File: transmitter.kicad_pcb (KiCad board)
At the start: 6 copper layers, 200 x 110 mm, 244 parts, among them IC1 W9864G6KH-6, IC2 TPS61165DBVR, IC3 MT25QL128ABA1ESE-0SIT, IC4 USBLC6-2SC6, J1 AFC01-S40FCA-00, J2 AFC07-S10ECC-00, J3 B2B-PH-K-S, J4 B2B-PH-K-S, J5 B3B-PH-K-S, J6 USB4085-GF-A, J7 Conn_01x05, J9 Conn_02x06_Odd_Even, Q1 AO3400A, Q2 AO3400A, Q3 SI2301CDS-T1-GE3, Q4 AO3400A, SW1 Button SPST SMD Tactile Switch, SW2 Button SPST SMD Tactile Switch, SW3 Button SPST SMD Tactile Switch, SW4 Button SPST SMD Tactile Switch, SW5 Button SPST SMD Tactile Switch, SW6 Button SPST SMD Tactile Switch, SW7 SW_SPDT_MSM, SW8 Button SPST SMD Tactile Switch, SW9 RotaryEncoder_Switch, U1 STM32H743ZIT6TR, U2 CAT24C256, U3 MP2667GG-0000-Z, U4 AMS1117-3.3, U5 TPS61252DSG, U6 PCA9554APW, Y1 32.768KHZ, Y2 X322525MOB4SI-25MHz

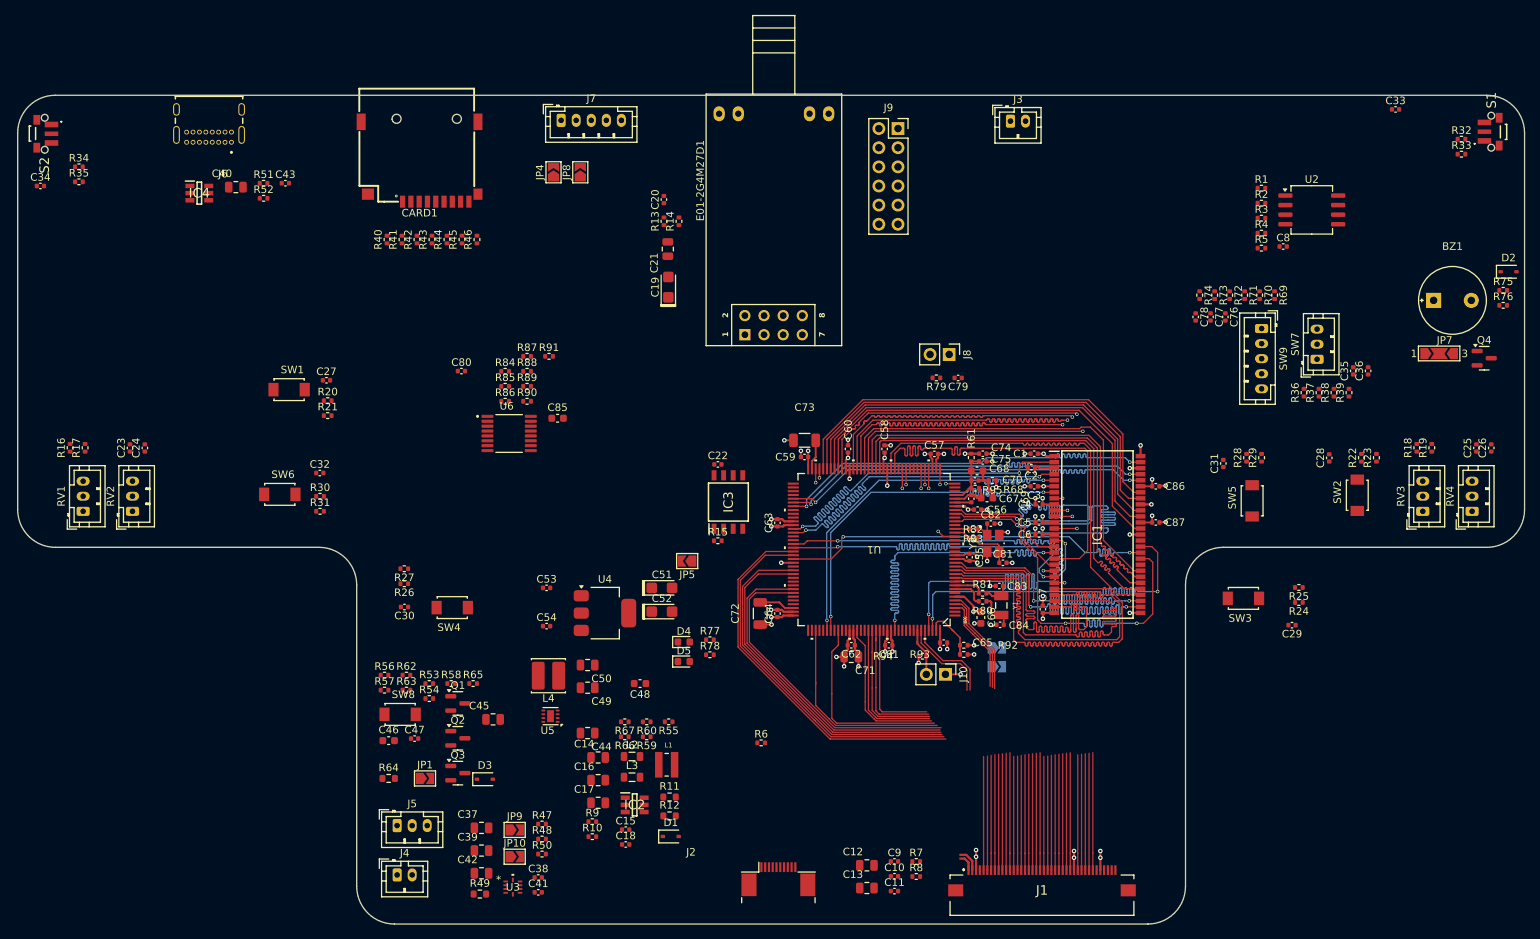
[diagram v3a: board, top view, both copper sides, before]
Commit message: duzo zmian, layout przetwornic i zasilania, wstepny routing sd card impedance control, usb differential impedance control
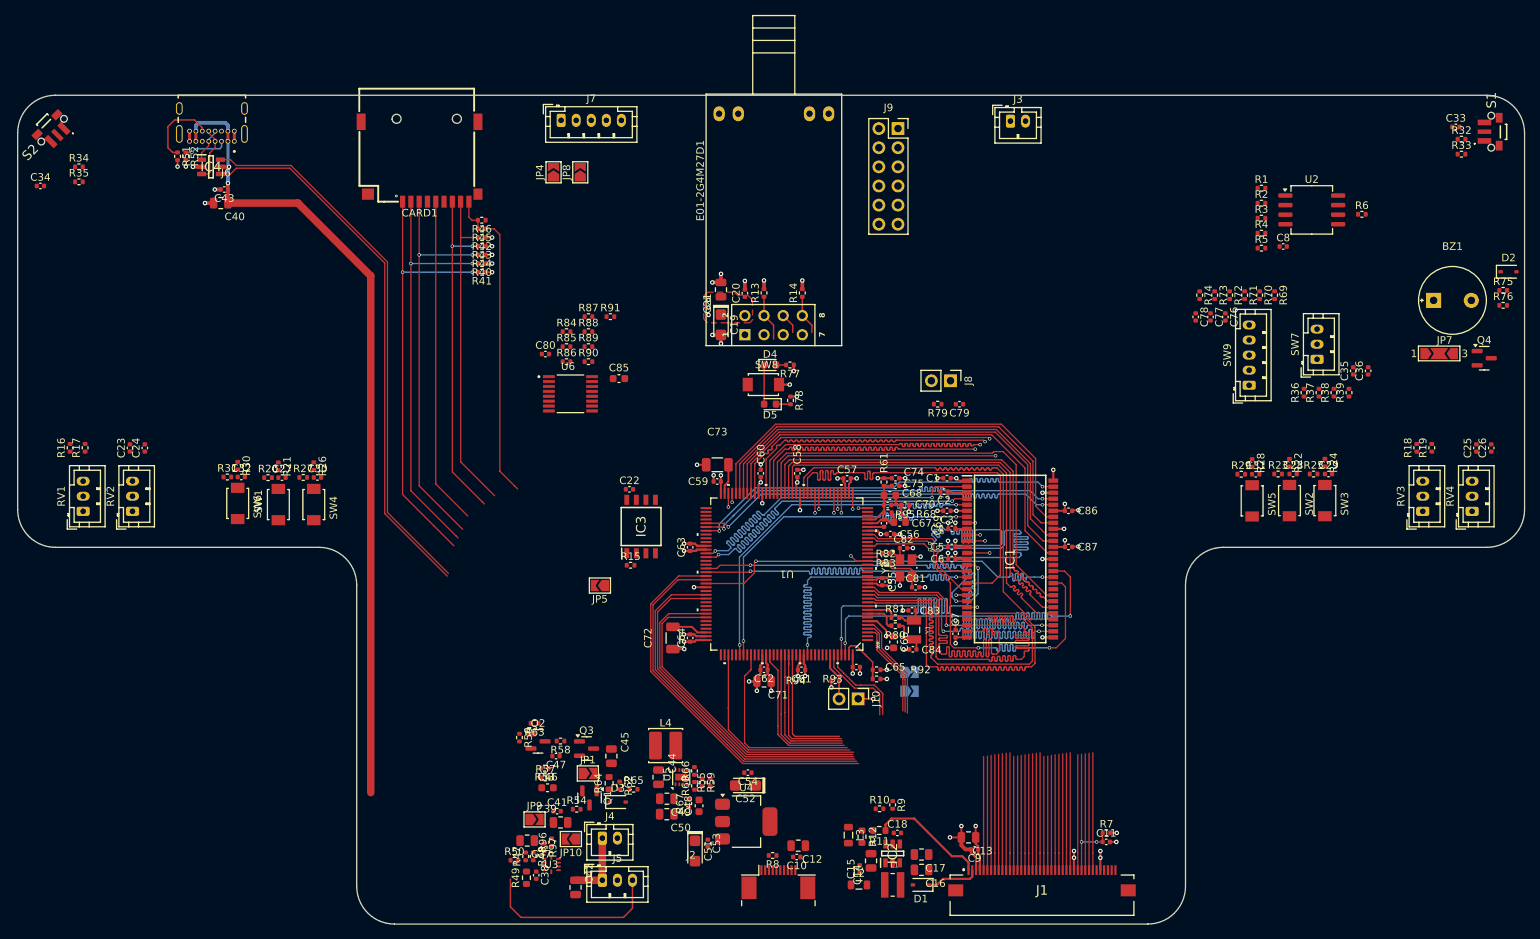
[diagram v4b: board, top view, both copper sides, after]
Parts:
- added R96: 0Ω, 0_resistors:R_0402_1005Metric, F.Cu at (92.4, 120.7)
- added R97: 0Ω, 0_resistors:R_0402_1005Metric, F.Cu at (91.4, 121.3)
- moved R6 106.2 mm to (199.9, 37.3)
- moved SW8 65.1 mm to (120.5, 59.9)
- moved C16 44.5 mm to (141.5, 124.3), turned to 180 degrees
- moved C17 43.5 mm to (141.5, 122.3), turned to 180 degrees
- moved C53 40.1 mm to (113.1, 120.8), turned to -90 degrees
- moved R9 39.9 mm to (137.6, 115.7), turned to -90 degrees
- moved C14 38.7 mm to (134.8, 123.1), turned to 90 degrees
- moved D4 38.5 mm to (121.4, 57.3)
- moved R10 38.3 mm to (135.9, 116.2)
- moved R77 38.0 mm to (124.0, 57.3), turned to 180 degrees
- moved C18 36.1 mm to (138.3, 119.4)
- moved D5 36.0 mm to (121.4, 62.5), turned to 180 degrees
- moved R78 35.4 mm to (124.1, 62.0), turned to -90 degrees
- moved C51 35.2 mm to (111.4, 121.8), turned to -90 degrees
- moved IC2 34.8 mm to (137.6, 122.1), turned to 90 degrees
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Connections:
- net /Project Architecture/Interface - USB FS/DM renamed /Project Architecture/Interface - USB FS/DN
- net /Project Architecture/Interface - USB FS/USB_OTG_FS_DM renamed /Project Architecture/Interface - USB FS/USB_OTG_FS_DN
- net /Project Architecture/LCD - Connectors/CTP_IRQ renamed /Project Architecture/Auxiliary/CTP_IRQ
- C79 pad 1: /Project Architecture/CTP_RESET -> /Project Architecture/Auxiliary/NRST
- CARD1 pad 7: /Project Architecture/MCU - IO/SDMMC2_CK -> /Project Architecture/MCU - IO/SDMMC2_D0
- J2 pad 3: /Project Architecture/LCD - Connectors/CTP_RESET -> /Project Architecture/Auxiliary/NRST
- J7 pad 4: /Project Architecture/CTP_RESET -> /Project Architecture/Auxiliary/NRST
- J8 pad 1: /Project Architecture/CTP_RESET -> /Project Architecture/Auxiliary/NRST
- J9 pad 1: /Project Architecture/Auxiliary/PB13 -> +5V
- J9 pad 3: /Project Architecture/Auxiliary/PG2 -> +3.3V
- R43 pad 2: /Project Architecture/MCU - IO/SDMMC2_CK -> /Project Architecture/MCU - IO/SDMMC2_D0
- R5 pad 2: /Project Architecture/LCD - Connectors/I2C3_SDA -> /Project Architecture/Memory - EEPROM/I2C3_SDA
- R6 pad 2: /Project Architecture/LCD - Connectors/I2C3_SCL -> /Project Architecture/Memory - EEPROM/I2C3_SCL
- R79 pad 2: /Project Architecture/CTP_RESET -> /Project Architecture/Auxiliary/NRST
- R87 pad 1: /Project Architecture/I2C3_SDA -> /Project Architecture/Auxiliary/I2C3_SDA
- R88 pad 1: /Project Architecture/I2C3_SCL -> /Project Architecture/Auxiliary/I2C3_SCL
- R89 pad 2: /Project Architecture/I2C3_SCL -> /Project Architecture/Auxiliary/I2C3_SCL
- R90 pad 2: /Project Architecture/I2C3_SDA -> /Project Architecture/Auxiliary/I2C3_SDA
- SW9 pad 1: (no net) -> Net-(R69-Pad2)
- SW9 pad 2: (no net) -> Net-(R70-Pad2)
- SW9 pad 3: (no net) -> GND
- SW9 pad 4: (no net) -> Net-(C78-Pad1)
- SW9 pad 5: (no net) -> GND
- U1 pad 100: /Project Architecture/LCD - Connectors/I2C3_SCL -> /Project Architecture/MCU - IO/I2C3_SCL
- U1 pad 25: /Project Architecture/CTP_RESET -> /Project Architecture/Auxiliary/NRST
- U1 pad 74: /Project Architecture/Auxiliary/PB13 -> /Project Architecture/MCU - IO/CD
- U1 pad 75: /Project Architecture/MCU - IO/SDMMC2_CK -> /Project Architecture/MCU - IO/SDMMC2_D0
- U1 pad 87: /Project Architecture/Auxiliary/PG2 -> /Project Architecture/Interface - RF Transmitter/RF_IRQ
- U1 pad 99: /Project Architecture/LCD - Connectors/I2C3_SDA -> /Project Architecture/MCU - IO/I2C3_SDA
- U3 pad 1: VBUS -> Net-(U3-IN)
- U3 pad 10: VSYS -> Net-(U3-SYS)
- U3 pad 6: /Project Architecture/I2C3_SCL -> /Project Architecture/Power - Charging/I2C3_SCL
- U3 pad 7: /Project Architecture/I2C3_SDA -> /Project Architecture/Power - Charging/I2C3_SDA
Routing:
- net VBUS: track 0.00 -> 109.9 mm, vias 0 -> 2
- net /Project Architecture/Interface - USB FS/USB_OTG_FS_DN: track 0.00 -> 72.5 mm
- net /Project Architecture/Interface - USB FS/USB_OTG_FS_DP: track 0.00 -> 72.3 mm
- net /Project Architecture/MCU - IO/SDMMC2_D2: track 0.00 -> 58.5 mm, vias 0 -> 2
- net /Project Architecture/MCU - IO/SDMMC2_D3: track 0.00 -> 56.1 mm, vias 0 -> 2
- net /Project Architecture/MCU - IO/SDMMC2_CMD: track 0.00 -> 53.7 mm, vias 0 -> 2
- net /Project Architecture/MCU - IO/SDMMC2_D0: track 0.00 -> 45.3 mm, vias 0 -> 2
- net /Project Architecture/MCU - IO/SDMMC2_CK: track 0.00 -> 43.5 mm
- net /Project Architecture/MCU - IO/SDMMC2_D1: track 0.00 -> 43.2 mm
- net /Project Architecture/MCU - IO/CD: track 0.00 -> 36.9 mm
- net /Project Architecture/Power - Battery/NTC_BATT: track 0.00 -> 24.7 mm
- net GND: track 66.5 -> 88.7 mm, vias 49 -> 62
- net +3.3V: track 59.1 -> 73.5 mm, vias 23 -> 36
- net /Project Architecture/LCD - Backlight/LCD_BACKLIGHT_V-: track 2.33 -> 15.6 mm
- net Net-(J6-CC2): track 0.00 -> 10.2 mm
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- added copper zone on F.Cu, net +3.3V

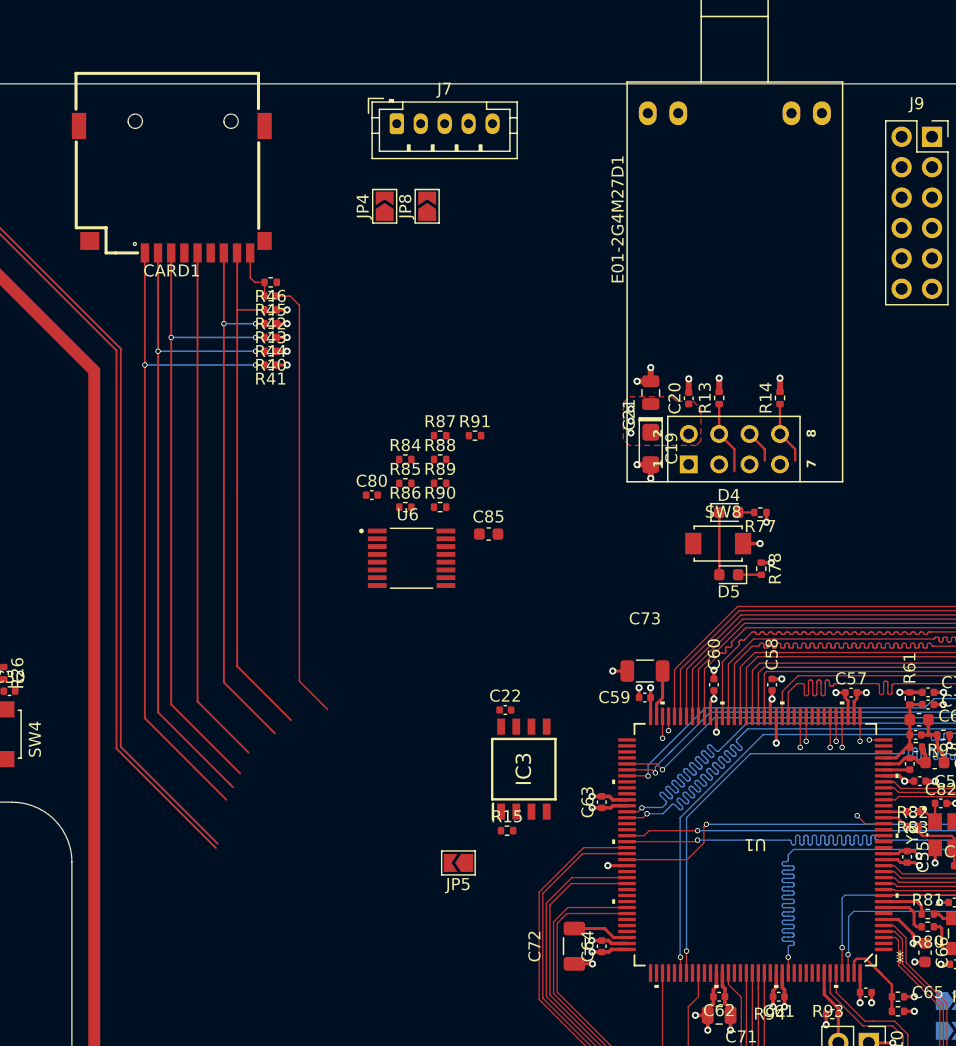
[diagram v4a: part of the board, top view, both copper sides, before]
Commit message: routed spi and signals to nrf24 rf module
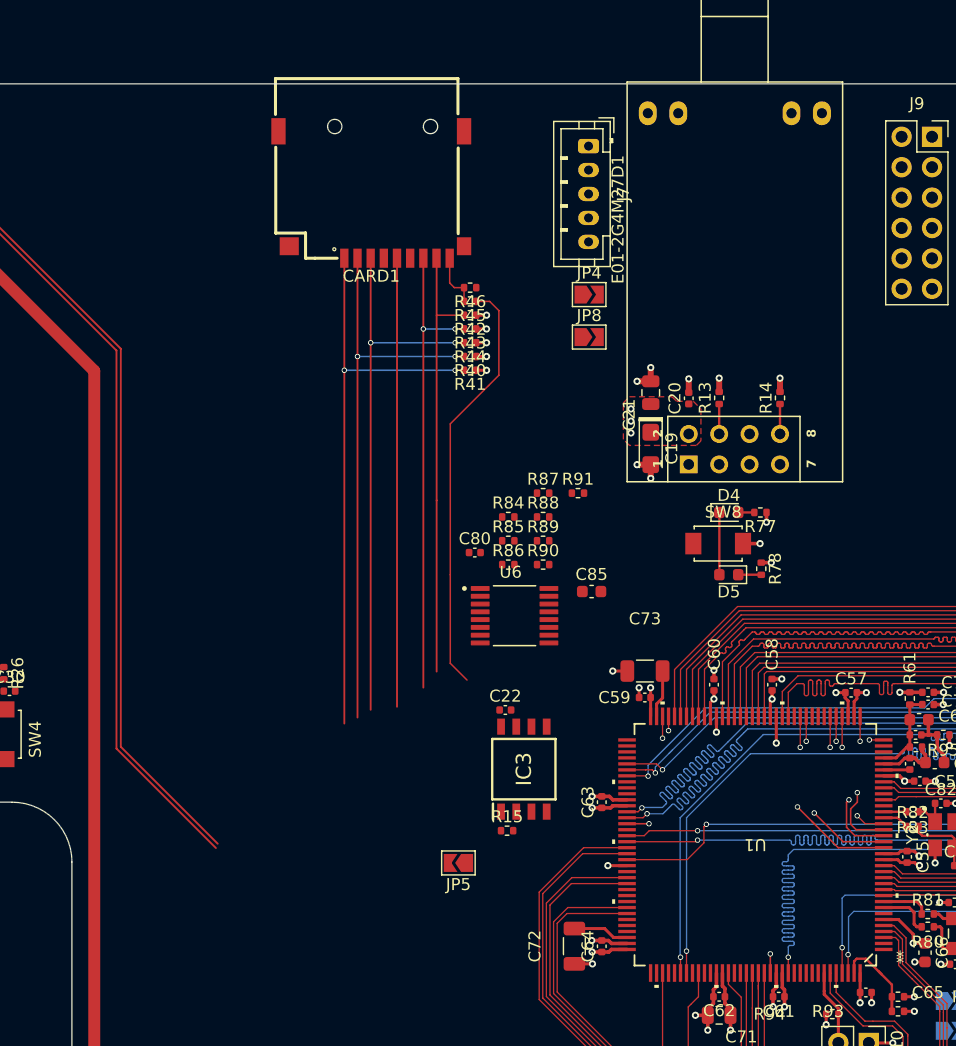
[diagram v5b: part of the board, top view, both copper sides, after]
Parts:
- moved JP4 18.6 mm to (109.7, 39.1), turned to 0 degrees
- moved JP8 17.4 mm to (109.7, 42.6), turned to 0 degrees
- moved R40 16.7 mm to (99.8, 44.3)
- moved R41 16.7 mm to (99.8, 45.4)
- moved R42 16.7 mm to (99.8, 40.8)
- moved R43 16.7 mm to (99.8, 42.0)
- moved R44 16.7 mm to (99.8, 43.1)
- moved R45 16.7 mm to (99.8, 39.7)
- moved R46 16.7 mm to (99.8, 38.5)
- moved CARD1 16.7 mm to (91.5, 30.8)
- moved J7 16.1 mm to (109.7, 26.7), turned to -90 degrees
- moved R87 9.85 mm to (105.9, 55.7)
- moved R90 9.85 mm to (105.9, 61.7)
- moved C80 9.85 mm to (100.2, 60.6)
- moved R88 9.85 mm to (105.9, 57.7)
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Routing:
- net /Project Architecture/Interface - RF Transmitter/RF_CE: track 0.00 -> 47.6 mm, vias 0 -> 1
- net /Project Architecture/Interface - RF Transmitter/RF_IRQ: track 5.25 -> 48.6 mm, vias 0 -> 1
- net /Project Architecture/Interface - RF Transmitter/SPI5_NSS: track 6.14 -> 47.5 mm, vias 0 -> 1
- net /Project Architecture/Interface - RF Transmitter/SPI5_SCK: track 0.00 -> 39.5 mm, vias 0 -> 1
- net /Project Architecture/Interface - RF Transmitter/SPI5_MOSI: track 2.75 -> 40.9 mm, vias 0 -> 1
- net /Project Architecture/Interface - RF Transmitter/SPI5_MISO: track 0.00 -> 36.2 mm, vias 0 -> 1
- net /Project Architecture/MCU - IO/SDMMC2_D2: track 58.5 -> 48.9 mm
- net /Project Architecture/MCU - IO/SDMMC2_D3: track 56.1 -> 47.3 mm
- net /Project Architecture/MCU - IO/SDMMC2_CMD: track 53.7 -> 45.5 mm
- net /Project Architecture/MCU - IO/SDMMC2_D1: track 43.2 -> 36.8 mm
- net /Project Architecture/MCU - IO/SDMMC2_D0: track 45.3 -> 39.3 mm
- net /Project Architecture/MCU - IO/SDMMC2_CK: track 43.5 -> 37.5 mm
- net /Project Architecture/MCU - IO/CD: track 36.9 -> 35.3 mm
- net /Project Architecture/LCD - Connectors/LTDC_R3: track 50.3 -> 51.7 mm
- net /Project Architecture/LCD - Connectors/LTDC_R6: track 51.0 -> 52.4 mm
